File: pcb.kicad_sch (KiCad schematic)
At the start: 26 parts

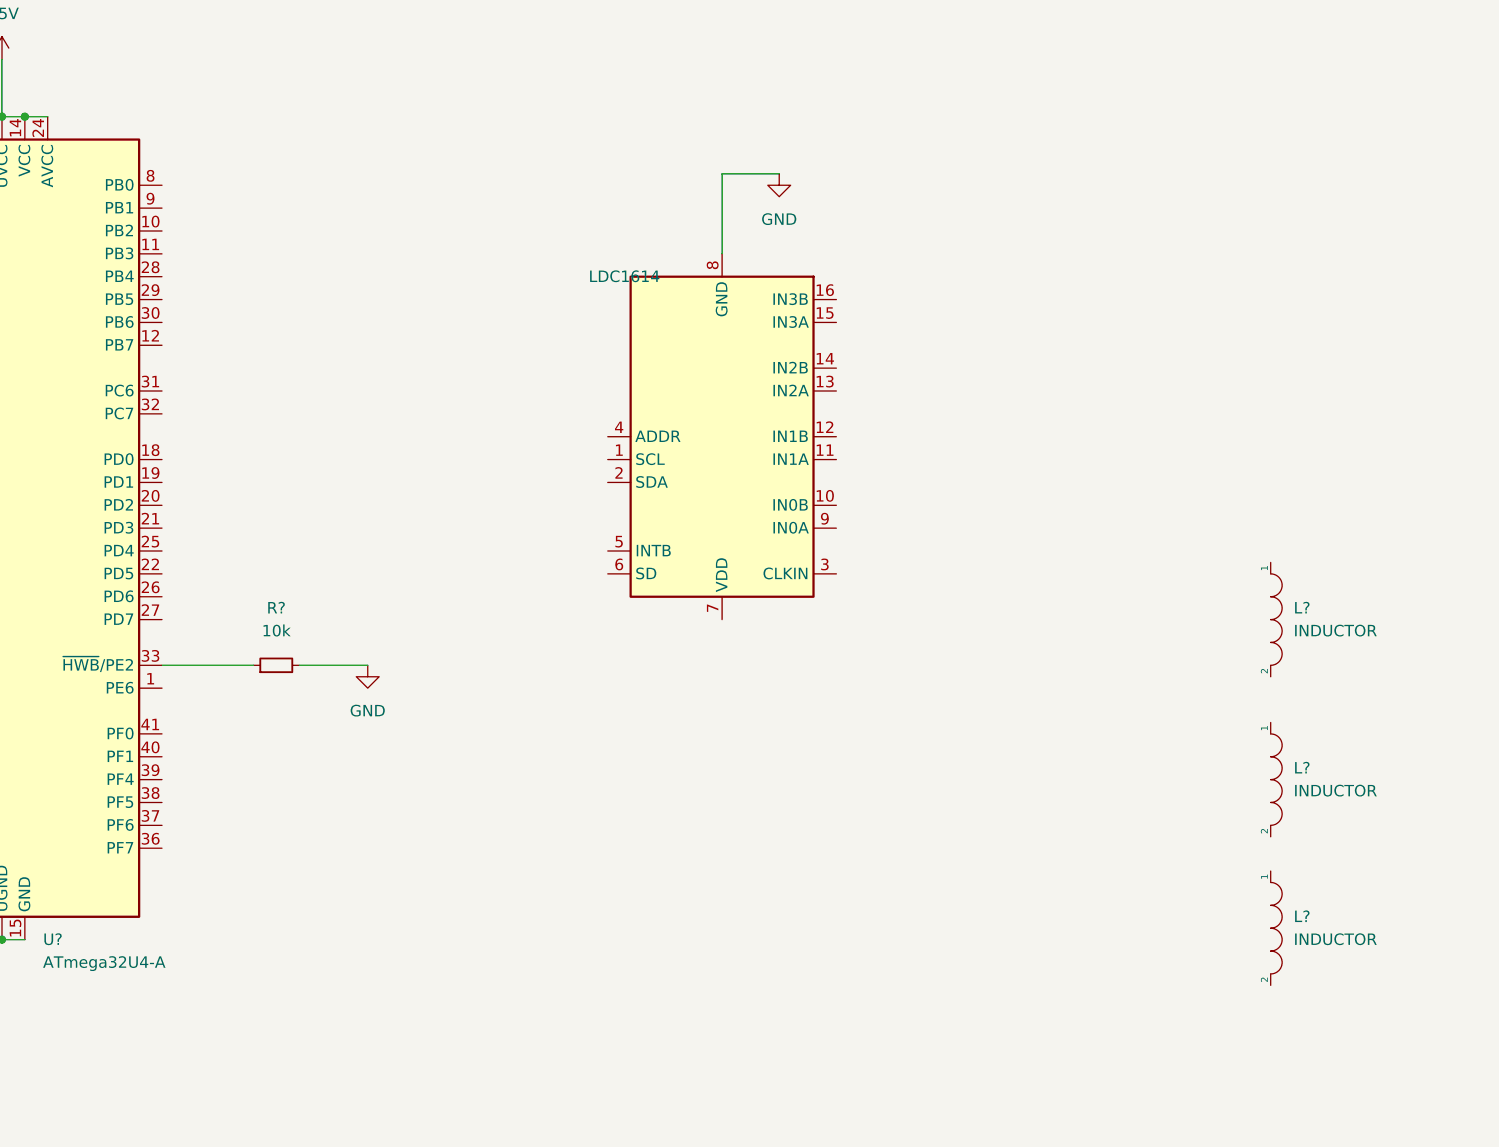
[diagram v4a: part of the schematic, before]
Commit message: ldc wiring update
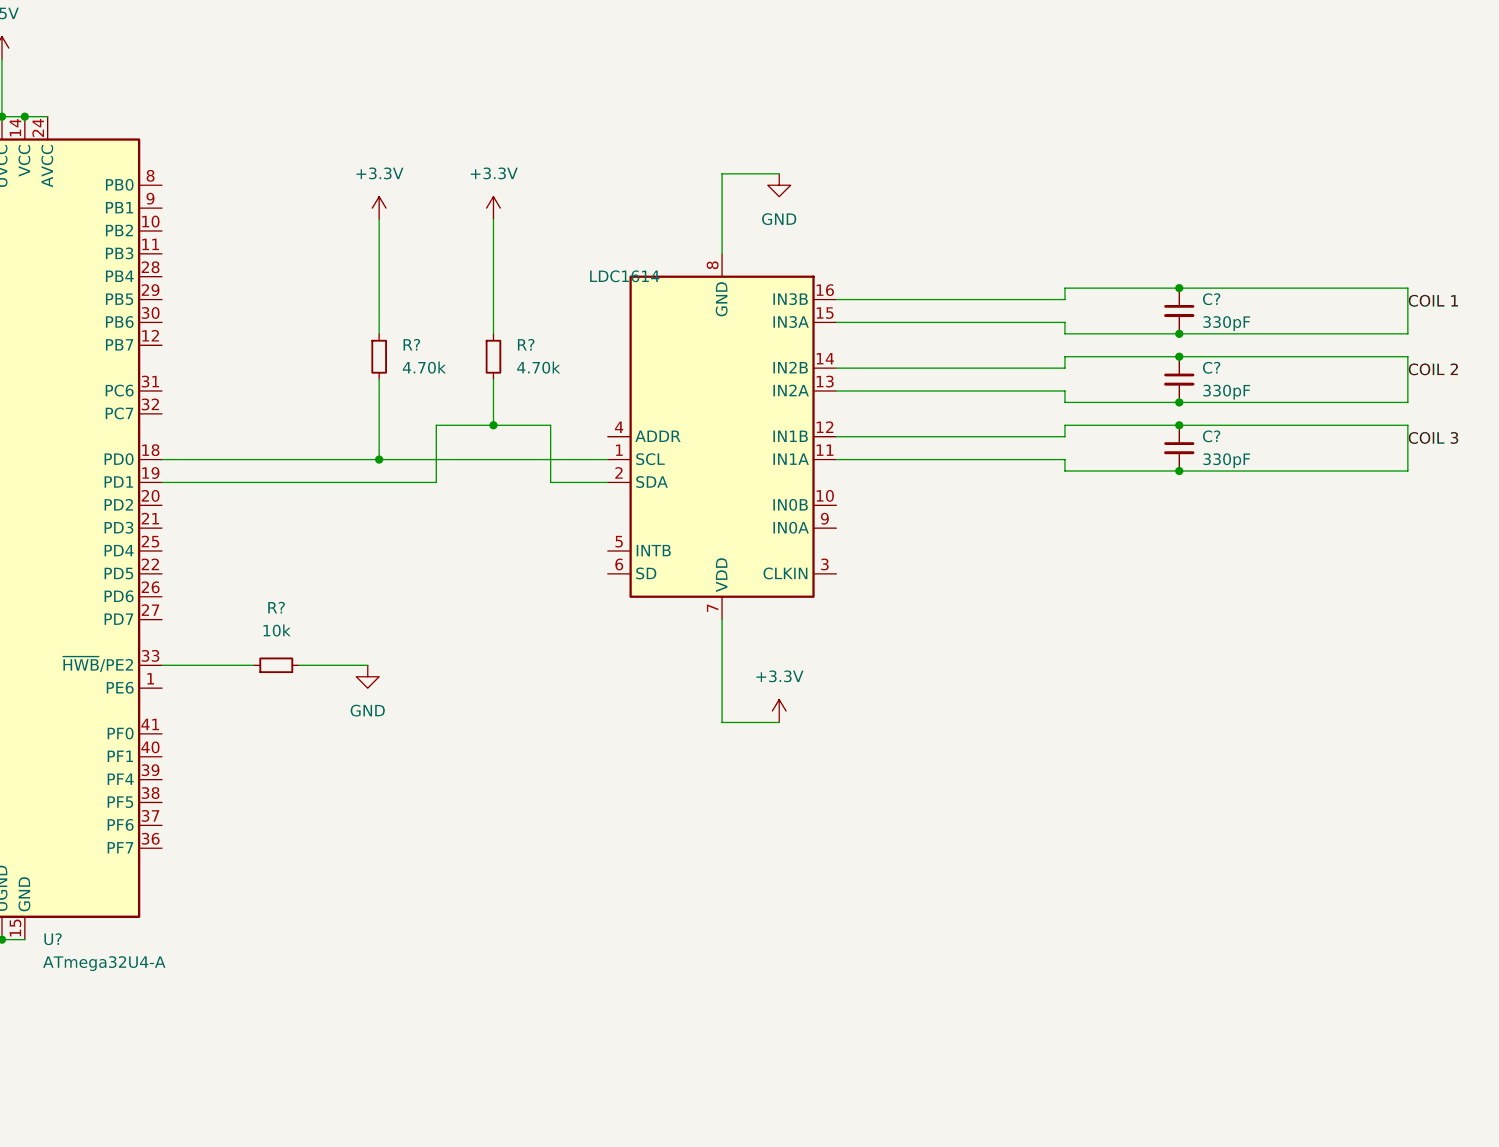
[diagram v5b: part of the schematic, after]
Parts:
- removed L? (x3): INDUCTOR, symbol pspice:INDUCTOR
- added C? (x3): 330pF, symbol Device:C_Small
- added R? (x2): 4.70k, symbol Device:R_Small
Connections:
- net +3.3V: now also U?.7 (VDD), R?.1, R?.1
- net at U?.1 (SCL): now also U?.18 (PD0), R?.2
- net COIL 3: now reaches U?.11 (IN1A)
- net COIL 3: now also U?.12 (IN1B), C?.1, C?.2
- net COIL 2: now reaches U?.13 (IN2A)
- net COIL 2: now also U?.14 (IN2B), C?.1, C?.2
- net COIL 1: now reaches U?.15 (IN3A)
- net COIL 1: now also U?.16 (IN3B), C?.1, C?.2
- net at U?.2 (SDA): now also U?.19 (PD1), R?.2

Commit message: schematic done v1
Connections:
- net +3.3V: now also U?.5 (INTB)
- net GND: now also U?.3 (CLKIN), U?.4 (ADDR), U?.6 (SD)
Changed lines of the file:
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@@
   (junction (at 215.9 66.04) (diameter 0) (color 0 0 0 0)
   )
+  (junction (at 148.59 90.17) (diameter 0) (color 0 0 0 0)
+  )
   (junction (at 41.91 59.69) (diameter 0) (color 0 0 0 0)
   )
@@
     (stroke (width 0) (type default) (color 0 0 0 0))
   )
+  (wire (pts (xy 148.59 74.93) (xy 148.59 90.17))
+    (stroke (width 0) (type default) (color 0 0 0 0))
+  )
   (wire (pts (xy 62.23 72.39) (xy 72.39 72.39))
     (stroke (width 0) (type default) (color 0 0 0 0))
@@
     (stroke (width 0) (type default) (color 0 0 0 0))
   )
+  (wire (pts (xy 139.7 87.63) (xy 152.4 87.63))
+    (stroke (width 0) (type default) (color 0 0 0 0))
+  )
+  (wire (pts (xy 152.4 74.93) (xy 148.59 74.93))
+    (stroke (width 0) (type default) (color 0 0 0 0))
+  )
   (wire (pts (xy 41.91 52.07) (xy 49.53 52.07))
     (stroke (width 0) (type default) (color 0 0 0 0))
@@
     (stroke (width 0) (type default) (color 0 0 0 0))
   )
+  (wire (pts (xy 177.8 90.17) (xy 194.31 90.17))
+    (stroke (width 0) (type default) (color 0 0 0 0))
+  )
   (wire (pts (xy 215.9 73.66) (xy 241.3 73.66))
     (stroke (width 0) (type default) (color 0 0 0 0))
@@
     (stroke (width 0) (type default) (color 0 0 0 0))
   )
+  (wire (pts (xy 148.59 90.17) (xy 148.59 101.6))
+    (stroke (width 0) (type default) (color 0 0 0 0))
+  )
   (wire (pts (xy 177.8 77.47) (xy 203.2 77.47))
     (stroke (width 0) (type default) (color 0 0 0 0))
@@
   )
   (wire (pts (xy 203.2 77.47) (xy 203.2 78.74))
+    (stroke (width 0) (type default) (color 0 0 0 0))
+  )
+  (wire (pts (xy 148.59 90.17) (xy 152.4 90.17))
     (stroke (width 0) (type default) (color 0 0 0 0))
   )
@@
     (pin "1")
     (pin "2")
+  )
+  (symbol (lib_id "power:+3.3V") (at 139.7 87.63 0) (unit 1)
+    (in_bom yes) (on_board yes) (fields_autoplaced)
+    (property "Reference" "#PWR?" (id 0) (at 139.7 91.44 0)
+      (effects (font (size 1.27 1.27)) hide)
+    )
+    (property "Value" "+3.3V" (id 1) (at 139.7 82.55 0))
+    (property "Footprint" "" (id 2) (at 139.7 87.63 0)
+      (effects (font (size 1.27 1.27)) hide)
+    )
+    (property "Datasheet" "" (id 3) (at 139.7 87.63 0)
+      (effects (font (size 1.27 1.27)) hide)
+    )
+    (pin "1")
   )
   (symbol (lib_id "power:GND") (at 152.4 175.26 0) (unit 1)
@@
     (pin "1")
   )
+  (symbol (lib_id "power:GND") (at 148.59 101.6 0) (unit 1)
+    (in_bom yes) (on_board yes) (fields_autoplaced)
+    (property "Reference" "#PWR?" (id 0) (at 148.59 107.95 0)
+      (effects (font (size 1.27 1.27)) hide)
+    )
+    (property "Value" "GND" (id 1) (at 148.59 106.68 0))
+    (property "Footprint" "" (id 2) (at 148.59 101.6 0)
+      (effects (font (size 1.27 1.27)) hide)
+    )
+    (property "Datasheet" "" (id 3) (at 148.59 101.6 0)
+      (effects (font (size 1.27 1.27)) hide)
+    )
+    (pin "1")
+  )
   (symbol (lib_id "random-keyboard-parts:PRTR5V0U2X") (at 91.44 175.26 0) (unit 1)
     (in_bom yes) (on_board yes)
@@
     )
     (property "Datasheet" "" (id 3) (at 85.09 33.02 0)
+      (effects (font (size 1.27 1.27)) hide)
+    )
+    (pin "1")
+  )
+  (symbol (lib_id "power:GND") (at 194.31 90.17 0) (unit 1)
+    (in_bom yes) (on_board yes) (fields_autoplaced)
+    (property "Reference" "#PWR?" (id 0) (at 194.31 96.52 0)
+      (effects (font (size 1.27 1.27)) hide)
+    )
+    (property "Value" "GND" (id 1) (at 194.31 95.25 0))
+    (property "Footprint" "" (id 2) (at 194.31 90.17 0)
+      (effects (font (size 1.27 1.27)) hide)
+    )
+    (property "Datasheet" "" (id 3) (at 194.31 90.17 0)
       (effects (font (size 1.27 1.27)) hide)
     )
@@
       (reference "#PWR?") (unit 1) (value "+5V") (footprint "")
     )
+    (path "/106d28f4-197d-41f1-b444-c9281c3572f6"
+      (reference "#PWR?") (unit 1) (value "+3.3V") (footprint "")
+    )
     (path "/16ffbb53-568c-4997-8847-97eb19764eb3"
       (reference "#PWR?") (unit 1) (value "GND") (footprint "")
@@
       (reference "#PWR?") (unit 1) (value "GND") (footprint "")
     )
+    (path "/94b1a700-7ae0-4ab1-b63f-d1666e754c87"
+      (reference "#PWR?") (unit 1) (value "GND") (footprint "")
+    )
     (path "/a4962e8d-3872-46dd-b3c7-6f1d496aec4b"
       (reference "#PWR?") (unit 1) (value "GND") (footprint "")
@@
       (reference "#PWR?") (unit 1) (value "+5V") (footprint "")
     )
+    (path "/acf2e171-c258-469d-aebc-5087763dc736"
+      (reference "#PWR?") (unit 1) (value "GND") (footprint "")
+    )
     (path "/b27e6389-be65-4c65-9fcf-abf1005836b3"
